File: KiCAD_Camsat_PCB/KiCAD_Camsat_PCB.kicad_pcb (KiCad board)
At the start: 2 copper layers, 50 parts, among them J3 105017-0001, J4 210-1S-1*3Ppin Gold-plated, J5 DZ127R-11-02-25, Q1 2N7002T-7-F, Q2 SS8050-G_C164885, Q8 2N7002T-7-F, Q9 SS8050-G_C164885, SW1 PTS645SH50SMTR92LFS, SW2 PTS645SH50SMTR92LFS, U5 DHT11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

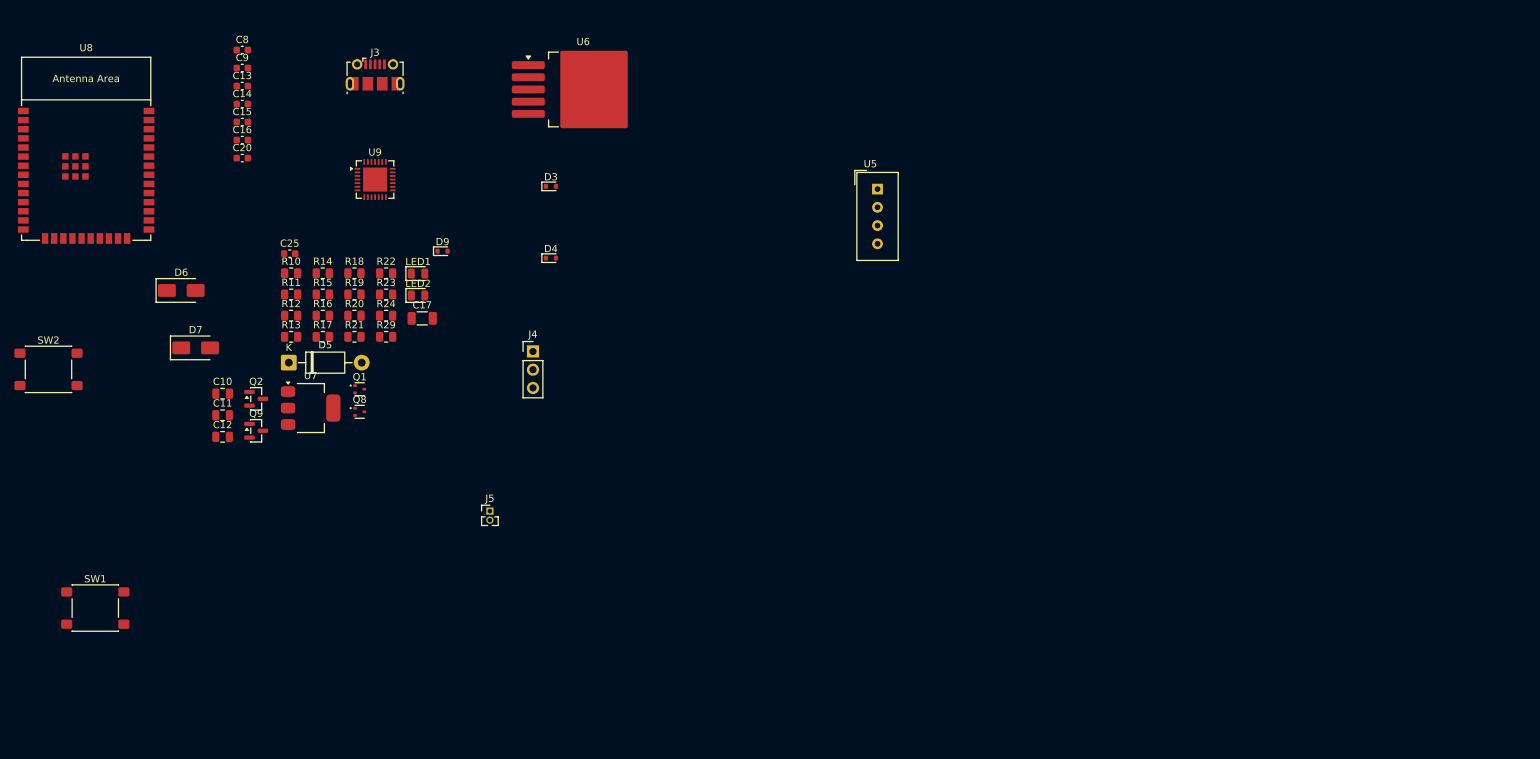
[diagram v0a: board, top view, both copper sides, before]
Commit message: schemaric errors
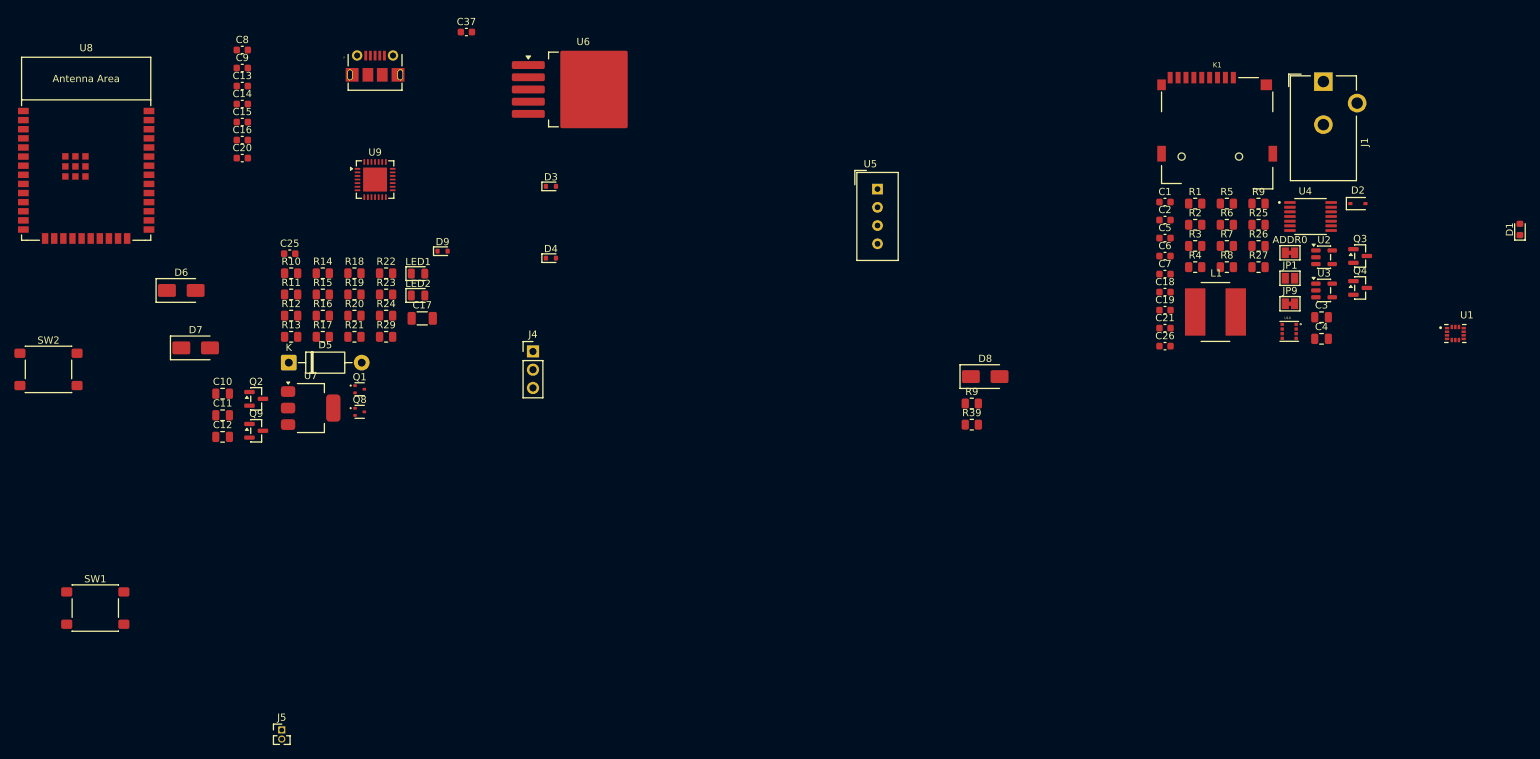
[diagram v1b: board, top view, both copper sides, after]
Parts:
- added ADDR0: JUMPER-SMT_3_1-NC_TRACE_SILK, Jumper:SolderJumper-2_P1.3mm_Bridged_Pad1.0x1.5mm, F.Cu at (193.5, 47.8)
- added C1: 2u2, Capacitor_SMD:C_0603_1608Metric, F.Cu at (176.1, 40.7)
- added C18: 100n, Capacitor_SMD:C_0603_1608Metric, F.Cu at (176.1, 53.2)
- added C19: 100n, Capacitor_SMD:C_0603_1608Metric, F.Cu at (176.1, 55.7)
- added C2: 2u2, Capacitor_SMD:C_0603_1608Metric, F.Cu at (176.1, 43.2)
- added C21: 100n, Capacitor_SMD:C_0603_1608Metric, F.Cu at (176.1, 58.2)
- added C26: 2u2, Capacitor_SMD:C_0603_1608Metric, F.Cu at (176.1, 60.8)
- added C3: 10uF, Capacitor_SMD:C_0805_2012Metric, F.Cu at (197.9, 56.7)
- added C37: 100nF, Capacitor_SMD:C_0603_1608Metric, F.Cu at (78.7, 17.0)
- added C4: 10uF, Capacitor_SMD:C_0805_2012Metric, F.Cu at (197.9, 59.7)
- added C5: 0.1uF, Capacitor_SMD:C_0603_1608Metric, F.Cu at (176.1, 45.7)
- added C6: 0.1uF, Capacitor_SMD:C_0603_1608Metric, F.Cu at (176.1, 48.2)
- added C7: 100n, Capacitor_SMD:C_0603_1608Metric, F.Cu at (176.1, 50.7)
- added D1: RED, LED_SMD:LED_0603_1608Metric, F.Cu at (225.5, 44.5)
- added D2: 1N4148, Diode_SMD:D_SOD-323, F.Cu at (202.9, 40.9)
- added D8: SS14, Diode_SMD:D_SMA, F.Cu at (151.0, 65.0)
- added J1: Barrel_Jack, Connector_BarrelJack:BarrelJack_CUI_PJ-102AH_Horizontal, F.Cu at (198.1, 23.9)
- added JP1: SMD_JUMPER, Jumper:SolderJumper-2_P1.3mm_Open_Pad1.0x1.5mm, F.Cu at (193.5, 51.3)
- added JP9: SMD-JUMPER-CONNECTED_TRACE_SLODERMASK, Jumper:SolderJumper-2_P1.3mm_Bridged_Pad1.0x1.5mm, F.Cu at (193.5, 54.9)
- added K1: HYC77-TF09-200, esp32:MICROSD-HYC77-TF09-200, F.Cu at (183.3, 31.1)
- added L1: 33uH, Inductor_SMD:L_Bourns_SRN8040TA, F.Cu at (183.1, 56.0)
- added Q3: BSS138, Package_TO_SOT_SMD:SOT-23, F.Cu at (203.2, 48.2)
- added Q4: BSS138, Package_TO_SOT_SMD:SOT-23, F.Cu at (203.2, 52.6)
- added R1: 10k, Resistor_SMD:R_0805_2012Metric, F.Cu at (180.3, 40.9)
- added R2: 2.2k, Resistor_SMD:R_0805_2012Metric, F.Cu at (180.3, 43.9)
- added R25: 2.2k, Resistor_SMD:R_0805_2012Metric, F.Cu at (189.1, 43.9)
- added R26: 10K, Resistor_SMD:R_0805_2012Metric, F.Cu at (189.1, 46.8)
- added R27: 10K, Resistor_SMD:R_0805_2012Metric, F.Cu at (189.1, 49.8)
- added R3: 10k, Resistor_SMD:R_0805_2012Metric, F.Cu at (180.3, 46.8)
- added R39: 10K, Resistor_SMD:R_0805_2012Metric, F.Cu at (149.1, 71.7)
- added R4: 1k, Resistor_SMD:R_0805_2012Metric, F.Cu at (180.3, 49.8)
- added R5: 10k, Resistor_SMD:R_0805_2012Metric, F.Cu at (184.7, 40.9)
- added R6: 10k, Resistor_SMD:R_0805_2012Metric, F.Cu at (184.7, 43.9)
- added R7: 10K, Resistor_SMD:R_0805_2012Metric, F.Cu at (184.7, 46.8)
- added R8: 10K, Resistor_SMD:R_0805_2012Metric, F.Cu at (184.7, 49.8)
- added R9: 10K, Resistor_SMD:R_0805_2012Metric, F.Cu at (149.1, 68.8)
- added R9: 10K, Resistor_SMD:R_0805_2012Metric, F.Cu at (189.1, 40.9)
- added U1: ISM330DHCX, esp32:PQFN50P250X300X86-14N, F.Cu at (216.5, 59.0)
- added U10: BME280, esp32:PSON65P250X250X100-8N, F.Cu at (193.4, 58.7)
- added U2: MIC5225-3.3, Package_TO_SOT_SMD:SOT-23-5, F.Cu at (198.2, 48.4)
- added U3: SE5218, Package_TO_SOT_SMD:SOT-23-5, F.Cu at (198.2, 53.0)
- added U4: TXB0104QPWRQ1, esp32:SOP65P640X120-14N, F.Cu at (196.3, 42.7)
- J3: footprint Connector_USB:USB_Micro-B_Molex-105017-0001 -> esp32:MOLEX_105017-0001
- moved J5 42.1 mm to (53.0, 114.2)
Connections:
- net MISO_H renamed /IO19
- net SCLK_H renamed /IO18
- C10 pad 1: +5V -> /5V_Board
- U7 pad 3: +5V -> /5V_Board
- U8 pad 16: MOSI_H -> /IO13
- U8 pad 29: CS_H -> /IO5
